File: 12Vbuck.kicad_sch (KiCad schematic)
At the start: 0 parts

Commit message: pågebynt 24V
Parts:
- added U1: LM5146RGYR, LM5146RGYR:IC_LM5146RGYR, symbol LM5146RGYR:LM5146RGYR
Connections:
- new net: U1.16 (NC), U1.9 (NC)
- new net EP: U1.15 (EP), U1.21 (EP)

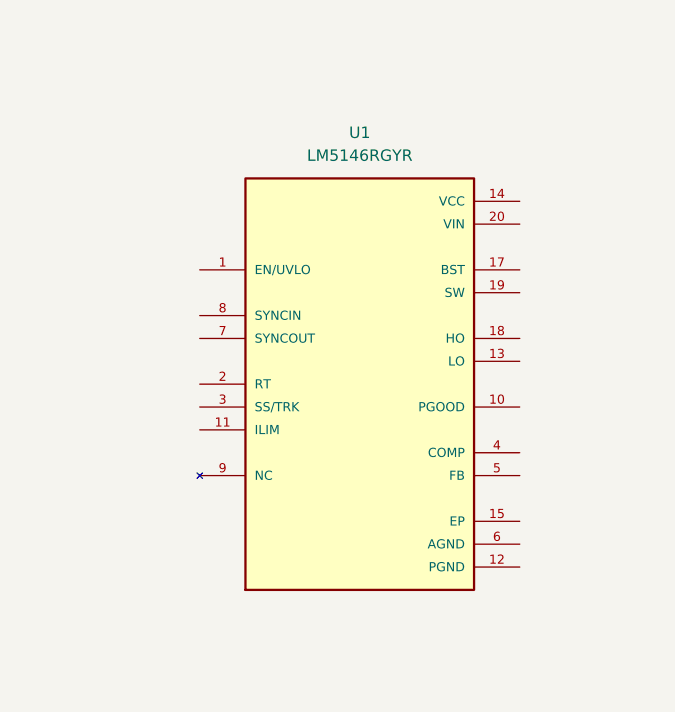
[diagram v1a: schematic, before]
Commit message: Fix 12V buck schematic merge conflict
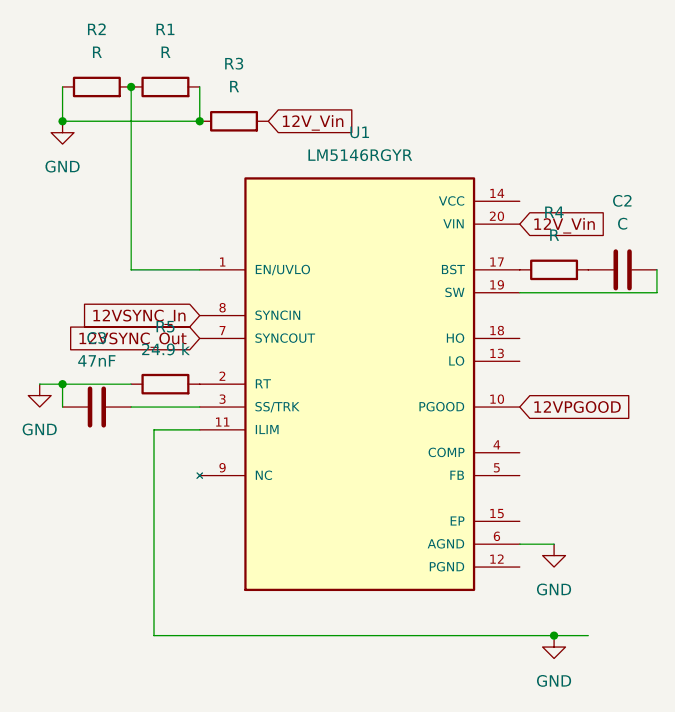
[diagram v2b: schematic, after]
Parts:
- added C2: C, symbol Device:C
- added C3: 47nF, symbol Device:C
- added R1, R2, R3, R4: R, symbol Device:R
- added R5: 24.9 k, symbol Device:R
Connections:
- net at U1.1 (EN/UVLO): now also R1.1, R2.2
- net 12VPGOOD: now reaches U1.10 (PGOOD)
- net GND: now reaches U1.11 (ILIM)
- net GND: now also U1.6 (AGND), C3.1, R1.2, R2.1, R3.1, R5.1
- net at U1.17 (BST): now also R4.1
- net at U1.19 (SW): now also C2.2
- net at U1.2 (RT): now also R5.2
- net 12V_Vin: now reaches U1.20 (VIN)
- net 12V_Vin: now also R3.2
- net at U1.3 (SS/TRK): now also C3.2
- net 12VSYNC_Out: now reaches U1.7 (SYNCOUT)
- net 12VSYNC_In: now reaches U1.8 (SYNCIN)
- new net: C2.1, R4.2

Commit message: jobb med 12V konverter
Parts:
- added C_C1: 4.7n, symbol Device:C
- added C_C2: 100p, symbol Device:C
- added C_C3: 1n, symbol Device:C
- added C_Vin: 0.1u, symbol Device:C
- added R_C1: 8.06k, symbol Device:R
- added R_C2: 100k, symbol Device:R
- added R_FB1: 1.5k, symbol Device:R
- added R_FB1: 21k, symbol Device:R
- C_BST: renamed from C2; value C -> 0.1u
- R_BST: renamed from R4; value R -> 2.2
- R_UV1: renamed from R1; value R -> 100k
- R_UV2: renamed from R2; value R -> 9.31k
- R_Vin: renamed from R3; value R -> 2.2
- renumbered C3 to C_ss, R5 to R_RT
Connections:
- net 12V_Vin: no longer U1.20 (VIN)
- net GND: now also C_Vin.1, R_FB1.2; no longer R_UV1.2, R_Vin.1
- new net: C_C2.2, C_C3.1, R_C1.2, R_C2.2, R_FB1.1
- new net: C_C1.2, C_C2.1
- new net: C_Vin.2, R_UV1.2, R_Vin.1, U1.20 (VIN)
- new net: C_C3.2, R_FB1.1
- new net: R_C2.1, R_FB1.2
- new net: C_C1.1, R_C1.1
- no-connect marks 0 -> 1

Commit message: jobbing med 5V og 12V
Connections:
- net 12VPGOOD renamed 12V_PGOOD
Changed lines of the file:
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@@
 		)
 	)
-	(global_label "12VPGOOD"
+	(global_label "12V_PGOOD"
 		(shape input)
 		(at 138.43 104.14 0)
@@
 		)
 		(property "Intersheetrefs" "${INTERSHEET_REFS}"
-			(at 150.7396 104.14 0)
+			(at 151.7072 104.14 0)
 			(hide yes)
 			(show_name no)
@@
 		(dnp no)
 		(property "Reference" "R_RT"
-			(at 94.742 99.06 90)
-			(show_name no)
-			(do_not_autoplace no)
+			(at 93.98 99.06 90)
+			(show_name no)
+			(do_not_autoplace no)

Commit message: endret annoteringen
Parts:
- added C_ILIM: 10p, symbol Device:C
- added C_In, C_In1, C_In2, C_In3, C_In4: 2.2 u, symbol Device:C
- added C_Out, C_Out1, C_Out2, C_Out3, C_Out4: 22u, symbol Device:C
- added C_VCC: 2.2u, symbol Device:C
- added L1: L, Package_SO:SSOP-16_3.9x4.9mm_P0.635mm, symbol Device:L
- added Q1, Q2: NMOS, Package_DFN_QFN:Nordic_AQFN-94-1EP_7x7mm_P0.4mm, symbol Simulation_SPICE:NMOS
- added R_ILIM: 619, symbol Device:R
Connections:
- net 12V_Vin: now also C_In2.1, Q1.1 (D)
- net GND: now also U1.12 (PGND), C_ILIM.2, C_In.2, C_Out.2, C_VCC.2, Q2.3 (S); no longer U1.11 (ILIM)
- net FB: now reaches C_C2.2, C_C3.1, R_C1.2, R_C2.2, R_FB1.1
- net FB: now also U1.5 (FB)
- net Comp: now reaches C_C1.2, C_C2.1
- net Comp: now also U1.4 (COMP)
- net V_out: now reaches R_C2.1, R_FB1.2
- net V_out: now also C_Out4.1, L1.2
- net at C_BST.2, U1.19 (SW): now also L1.1, Q1.3 (S), Q2.1 (D), R_ILIM.2
- net at U1.13 (LO): now also Q2.2 (G)
- net at U1.14 (VCC): now also C_VCC.1
- net at U1.18 (HO): now also Q1.2 (G)
- new net: C_Out.1, C_Out1.2
- new net: C_Out1.1, C_Out2.2
- new net: C_Out3.1, C_Out4.2
- new net: C_Out2.1, C_Out3.2
- new net: C_In2.2, C_In3.1
- new net: C_In3.2, C_In4.1
- new net: C_In.1, C_In1.2
- new net: C_In1.1, C_In4.2
- new net: C_ILIM.1, R_ILIM.1, U1.11 (ILIM)
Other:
- moved on the sheet: C_C1, C_C2, C_C3, R_C1, R_C2, R_FB1
